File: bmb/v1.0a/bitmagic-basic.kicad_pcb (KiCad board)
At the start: 4 copper layers, 35 x 16 mm, 38 parts, among them IC1 CY7C68013A-56, J1 Conn, P1 pkl_USB_OTG, U1 3.3V, U2 USBLC6-2, U3 IP425x-4-TTL, U4 IP425x-4-TTL, U5 24LC00, U6 IP425x-4-TTL, X1 24MHz

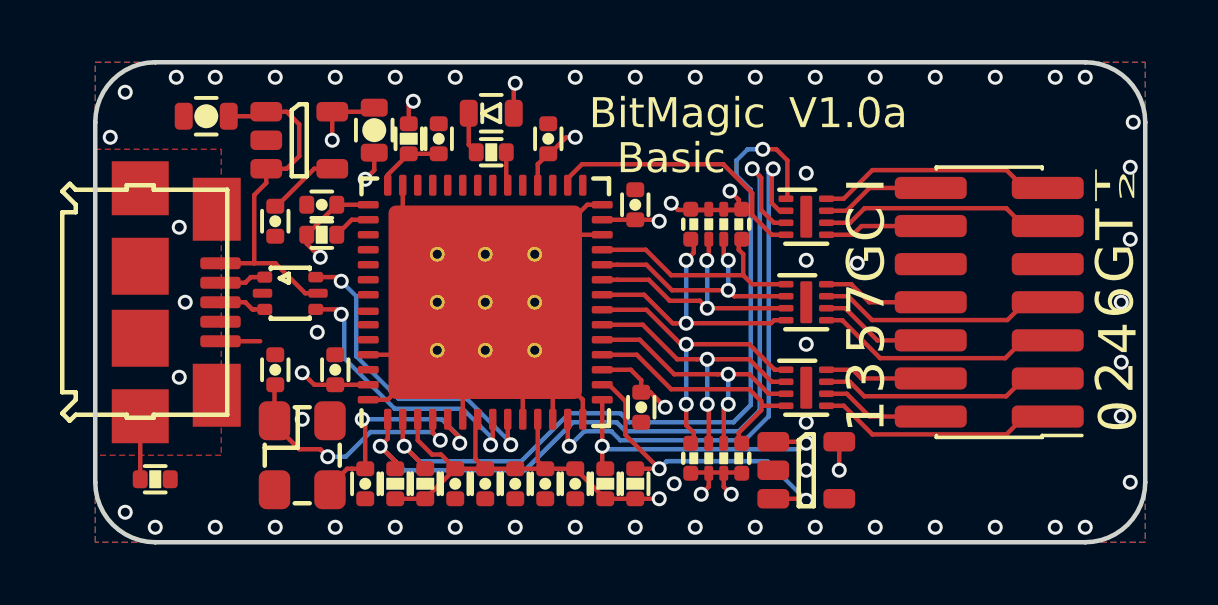
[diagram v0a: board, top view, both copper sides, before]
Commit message: Corrected 3d model paths.
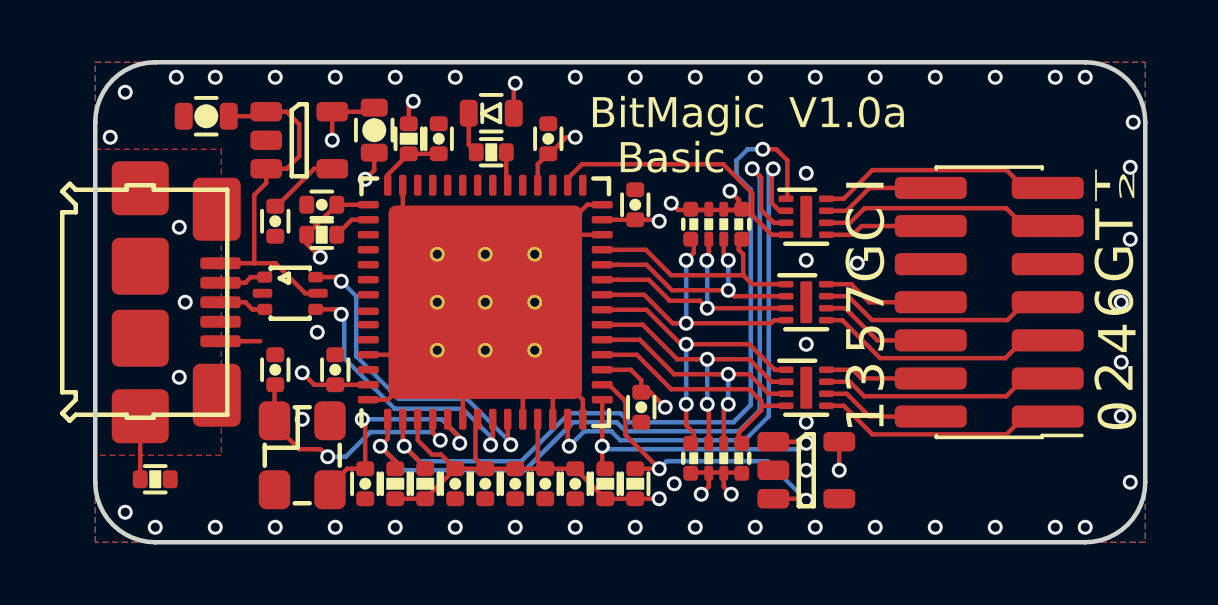
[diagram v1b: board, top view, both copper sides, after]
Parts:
- removed the REF** at (39.5, 30.5)
- added REF**: 1b2_Logo_SilkS_5mm, pkl_logos:1b2_Logo_SilkS_5mm, B.Cu at (35.2, 30.2)
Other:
- board text added: "&"
- board text added: "securing hardware.com"

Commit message: Minor updates.
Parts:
- removed REF**: 1b2_Logo_SilkS_5mm, pkl_logos:1b2_Logo_SilkS_5mm
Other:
- board text removed: "&"
- board text removed: "1BitSquared"
- board text removed: "securing hardware.com"
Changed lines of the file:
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@@
   (general
     (thickness 1.6)
-    (drawings 63)
+    (drawings 60)
     (tracks 472)
     (zones 0)
-    (modules 38)
+    (modules 37)
     (nets 42)
   )
@@
     (pad_to_mask_clearance 0.05)
     (aux_axis_origin 0 0)
-    (visible_elements FFFFFF7F)
+    (visible_elements FFFFFF1F)
     (pcbplotparams
       (layerselection 0x010fc_ffffffff)
@@
     (add_net "Net-(U5-Pad4)")
   )
-  (module pkl_logos:1b2_Logo_SilkS_5mm locked (layer B.Cu)
-    (at 35.2 30.2 90)
-    (fp_text reference REF** (at 0 -6 90) (layer B.Fab) hide
-      (effects (font (size 1 1) (thickness 0.15)) (justify mirror))
-    )
-    (fp_text value 1b2_Logo_SilkS_5mm (at 0 6.35 90) (layer B.Fab) hide
-      (effects (font (size 1 1) (thickness 0.15)) (justify mirror))
-    )
-    (fp_line (start -0.5 0.5) (end -0.5 2.5) (layer B.SilkS) (width 0.2))
-    (fp_line (start -0.5 2.5) (end -2.5 2.5) (layer B.SilkS) (width 0.2))
-    (fp_line (start -2.5 2.5) (end -2.5 0.5) (layer B.SilkS) (width 0.2))
-    (fp_line (start -2.5 0.5) (end -0.5 0.5) (layer B.SilkS) (width 0.2))
-    (fp_line (start -0.5 2.5) (end 0 2) (layer B.SilkS) (width 0.2))
-    (fp_line (start 0 2) (end 0 0) (layer B.SilkS) (width 0.2))
-    (fp_line (start 0 0) (end -0.5 0.5) (layer B.SilkS) (width 0.2))
-    (fp_line (start -2.5 0.5) (end -2 0) (layer B.SilkS) (width 0.2))
-    (fp_line (start -2 0) (end 0 0) (layer B.SilkS) (width 0.2))
-    (fp_line (start 2 2) (end 0.5 2) (layer B.SilkS) (width 0.2))
-    (fp_line (start 0.5 2) (end 0.5 -0.5) (layer B.SilkS) (width 0.2))
-    (fp_line (start 0.5 -0.5) (end -2 -0.5) (layer B.SilkS) (width 0.2))
-    (fp_line (start -2 -0.5) (end -2 -2) (layer B.SilkS) (width 0.2))
-    (fp_line (start -2 -2) (end 2 -2) (layer B.SilkS) (width 0.2))
-    (fp_line (start 2 -2) (end 2 2) (layer B.SilkS) (width 0.2))
-    (fp_line (start 2 2) (end 2.5 1.5) (layer B.SilkS) (width 0.2))
-    (fp_line (start 2.5 1.5) (end 2.5 -2.5) (layer B.SilkS) (width 0.2))
-    (fp_line (start 2.5 -2.5) (end 2 -2) (layer B.SilkS) (width 0.2))
-    (fp_line (start -2 -2) (end -1.5 -2.5) (layer B.SilkS) (width 0.2))
-    (fp_line (start -1.5 -2.5) (end 2.5 -2.5) (layer B.SilkS) (width 0.2))
-  )
   (module pkl_misc:ABM8 (layer F.Cu)
     (at 28.9 35.1 270)
@@
     )
     (fp_text value Conn (at 0 5.505) (layer F.Fab)
+      (effects (font (size 1 1) (thickness 0.15)))
+    )
+    (fp_text user %R (at 0 0 90) (layer F.Fab)
       (effects (font (size 1 1) (thickness 0.15)))
     )
@@
     (fp_line (start -1.27 -4.445) (end 1.705 -4.445) (layer F.Fab) (width 0.1))
     (fp_line (start 1.705 4.445) (end -1.705 4.445) (layer F.Fab) (width 0.1))
-    (pad 14 smd roundrect (at 1.95 3.81 180) (size 2.4 0.74) (layers F.Cu F.Paste F.Mask) (roundrect_rratio 0.25)
+    (pad 14 smd rect (at 1.95 3.81 180) (size 2.4 0.74) (layers F.Cu F.Paste F.Mask)
       (net 37 /xIFCLK))
-    (pad 13 smd roundrect (at -1.95 3.81 180) (size 2.4 0.74) (layers F.Cu F.Paste F.Mask) (roundrect_rratio 0.25)
+    (pad 13 smd rect (at -1.95 3.81 180) (size 2.4 0.74) (layers F.Cu F.Paste F.Mask)
       (net 41 /xTRIG2))
-    (pad 12 smd roundrect (at 1.95 2.54 180) (size 2.4 0.74) (layers F.Cu F.Paste F.Mask) (roundrect_rratio 0.25)
+    (pad 12 smd rect (at 1.95 2.54 180) (size 2.4 0.74) (layers F.Cu F.Paste F.Mask)
       (net 36 /xCLK))
-    (pad 11 smd roundrect (at -1.95 2.54 180) (size 2.4 0.74) (layers F.Cu F.Paste F.Mask) (roundrect_rratio 0.25)
+    (pad 11 smd rect (at -1.95 2.54 180) (size 2.4 0.74) (layers F.Cu F.Paste F.Mask)
       (net 35 /xTRIG))
-    (pad 10 smd roundrect (at 1.95 1.27 180) (size 2.4 0.74) (layers F.Cu F.Paste F.Mask) (roundrect_rratio 0.25)
-      (net 2 GND))
-    (pad 9 smd roundrect (at -1.95 1.27 180) (size 2.4 0.74) (layers F.Cu F.Paste F.Mask) (roundrect_rratio 0.25)
-      (net 2 GND))
-    (pad 8 smd roundrect (at 1.95 0 180) (size 2.4 0.74) (layers F.Cu F.Paste F.Mask) (roundrect_rratio 0.25)
+    (pad 10 smd rect (at 1.95 1.27 180) (size 2.4 0.74) (layers F.Cu F.Paste F.Mask)
+      (net 2 GND))
+    (pad 9 smd rect (at -1.95 1.27 180) (size 2.4 0.74) (layers F.Cu F.Paste F.Mask)
+      (net 2 GND))
+    (pad 8 smd rect (at 1.95 0 180) (size 2.4 0.74) (layers F.Cu F.Paste F.Mask)
       (net 25 /xPB7))
-    (pad 7 smd roundrect (at -1.95 0 180) (size 2.4 0.74) (layers F.Cu F.Paste F.Mask) (roundrect_rratio 0.25)
+    (pad 7 smd rect (at -1.95 0 180) (size 2.4 0.74) (layers F.Cu F.Paste F.Mask)
       (net 26 /xPB6))
-    (pad 6 smd roundrect (at 1.95 -1.27 180) (size 2.4 0.74) (layers F.Cu F.Paste F.Mask) (roundrect_rratio 0.25)
+    (pad 6 smd rect (at 1.95 -1.27 180) (size 2.4 0.74) (layers F.Cu F.Paste F.Mask)
       (net 23 /xPB5))
-    (pad 5 smd roundrect (at -1.95 -1.27 180) (size 2.4 0.74) (layers F.Cu F.Paste F.Mask) (roundrect_rratio 0.25)
+    (pad 5 smd rect (at -1.95 -1.27 180) (size 2.4 0.74) (layers F.Cu F.Paste F.Mask)
       (net 24 /xPB4))
-    (pad 4 smd roundrect (at 1.95 -2.54 180) (size 2.4 0.74) (layers F.Cu F.Paste F.Mask) (roundrect_rratio 0.25)
+    (pad 4 smd rect (at 1.95 -2.54 180) (size 2.4 0.74) (layers F.Cu F.Paste F.Mask)
       (net 21 /xPB3))
-    (pad 3 smd roundrect (at -1.95 -2.54 180) (size 2.4 0.74) (layers F.Cu F.Paste F.Mask) (roundrect_rratio 0.25)
+    (pad 3 smd rect (at -1.95 -2.54 180) (size 2.4 0.74) (layers F.Cu F.Paste F.Mask)
       (net 22 /xPB2))
-    (pad 2 smd roundrect (at 1.95 -3.81 180) (size 2.4 0.74) (layers F.Cu F.Paste F.Mask) (roundrect_rratio 0.25)
+    (pad 2 smd rect (at 1.95 -3.81 180) (size 2.4 0.74) (layers F.Cu F.Paste F.Mask)
       (net 19 /xPB1))
-    (pad 1 smd roundrect (at -1.95 -3.81 180) (size 2.4 0.74) (layers F.Cu F.Paste F.Mask) (roundrect_rratio 0.25)
+    (pad 1 smd rect (at -1.95 -3.81 180) (size 2.4 0.74) (layers F.Cu F.Paste F.Mask)
       (net 20 /xPB0))
     (model ${KISYS3DMOD}/Connector_PinHeader_1.27mm.3dshapes/PinHeader_2x07_P1.27mm_Vertical_SMD.wrl
@@
     )
   )
-  (gr_text & (at 38.8 30 270) (layer B.SilkS)
-    (effects (font (size 1 1) (thickness 0.25)) (justify mirror))
-  )
-  (gr_text "securing\nhardware.com" (at 41.4 30 270) (layer B.SilkS)
-    (effects (font (size 1 1) (thickness 0.25)) (justify mirror))
-  )
   (gr_text G (at 56 28.7 90) (layer F.SilkS)
     (effects (font (size 1.25 1.25) (thickness 0.3)))
@@
     (effects (font (size 1 1) (thickness 0.25)))
   )
-  (gr_text "T\n2" (at 53.8 26.1 90) (layer B.SilkS)
+  (gr_text "T\n2" (at 53.8 26.1 270) (layer B.SilkS)
     (effects (font (size 0.5 1.25) (thickness 0.125)) (justify mirror))
   )
-  (gr_text 1BitSquared (at 31.3 30 270) (layer B.SilkS)
-    (effects (font (size 1 1) (thickness 0.25)) (justify mirror))
-  )
-  (gr_text I (at 49.8 26.1 90) (layer B.SilkS)
+  (gr_text I (at 49.6 26.1 270) (layer B.SilkS)
     (effects (font (size 1.25 1.25) (thickness 0.3)) (justify mirror))
   )
   (gr_line (start 51.8 26.1) (end 52.8 26.1) (layer B.SilkS) (width 0.2))
   (gr_line (start 51.8 26.1) (end 50.7 26.1) (layer B.SilkS) (width 0.2))
-  (gr_text 7 (at 49.8 29.9 90) (layer B.SilkS)
+  (gr_text 7 (at 49.6 29.9 270) (layer B.SilkS)
     (effects (font (size 1.25 1.25) (thickness 0.3)) (justify mirror))
   )
-  (gr_text C (at 49.8 27.4 90) (layer B.SilkS)
+  (gr_text C (at 49.6 27.4 270) (layer B.SilkS)
     (effects (font (size 1.25 1.25) (thickness 0.3)) (justify mirror))
   )
-  (gr_text G (at 49.8 28.7 90) (layer B.SilkS)
+  (gr_text G (at 49.6 28.7 270) (layer B.SilkS)
     (effects (font (size 1.25 1.25) (thickness 0.3)) (justify mirror))
   )
-  (gr_text G (at 53.8 28.7 90) (layer B.SilkS)
+  (gr_text G (at 53.8 28.7 270) (layer B.SilkS)
     (effects (font (size 1.25 1.25) (thickness 0.3)) (justify mirror))
   )
-  (gr_text T (at 53.8 27.4 90) (layer B.SilkS)
+  (gr_text T (at 53.8 27.4 270) (layer B.SilkS)
     (effects (font (size 1.25 1.25) (thickness 0.3)) (justify mirror))
   )
-  (gr_text 6 (at 53.8 30 90) (layer B.SilkS)
+  (gr_text 6 (at 53.8 30 270) (layer B.SilkS)
     (effects (font (size 1.25 1.25) (thickness 0.3)) (justify mirror))
   )
@@
   (gr_line (start 51.8 27.4) (end 52.8 27.4) (layer B.SilkS) (width 0.2))
   (gr_line (start 51.8 33.7) (end 51.8 26.1) (layer B.SilkS) (width 0.2))
-  (gr_text 4 (at 53.8 31.2 90) (layer B.SilkS)
+  (gr_text 4 (at 53.8 31.2 270) (layer B.SilkS)
     (effects (font (size 1.25 1.25) (thickness 0.3)) (justify mirror))
   )
-  (gr_text 5 (at 49.8 31.2 90) (layer B.SilkS)
+  (gr_text 5 (at 49.6 31.2 270) (layer B.SilkS)
     (effects (font (size 1.25 1.25) (thickness 0.3)) (justify mirror))
   )
-  (gr_text 3 (at 49.8 32.5 90) (layer B.SilkS)
+  (gr_text 3 (at 49.6 32.5 270) (layer B.SilkS)
     (effects (font (size 1.25 1.25) (thickness 0.3)) (justify mirror))
   )
-  (gr_text 2 (at 53.8 32.5 90) (layer B.SilkS)
+  (gr_text 2 (at 53.8 32.5 270) (layer B.SilkS)
     (effects (font (size 1.25 1.25) (thickness 0.3)) (justify mirror))
   )
-  (gr_text 1 (at 49.8 33.8 90) (layer B.SilkS)
+  (gr_text 1 (at 49.6 33.8 270) (layer B.SilkS)
     (effects (font (size 1.25 1.25) (thickness 0.3)) (justify mirror))
   )
-  (gr_text 0 (at 53.8 33.8 90) (layer B.SilkS)
+  (gr_text 0 (at 53.8 33.8 270) (layer B.SilkS)
     (effects (font (size 1.25 1.25) (thickness 0.3)) (justify mirror))
   )
@@
   (via (at 41.7 28.6) (size 0.5) (drill 0.3) (layers F.Cu B.Cu) (net 18))
   (via (at 56.2 32) (size 0.5) (drill 0.3) (layers F.Cu B.Cu) (net 2))
-  (via (at 47.4 28.7) (size 0.5) (drill 0.3) (layers F.Cu B.Cu) (net 2))
+  (via (at 47.4 28.6) (size 0.5) (drill 0.3) (layers F.Cu B.Cu) (net 2))
   (segment (start 46.375 33.05) (end 47.05 33.05) (width 0.15) (layer F.Cu) (net 19))
   (segment (start 47.81 33.81) (end 49.85 33.81) (width 0.15) (layer F.Cu) (net 19))
